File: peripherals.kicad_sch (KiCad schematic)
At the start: 39 parts, among them J12 PinHeader_2x5_P1.27mm_SMD, J13 PinHeader_2x5_P1.27mm_SMD, J14 PinHeader_2x5_P1.27mm_SMD, J15 PinHeader_2x5_P1.27mm_SMD, J16 PinHeader_2x5_P1.27mm_SMD, J20 PinHeader_2x5_P1.27mm_SMD, J6 PinHeader_2x10_P1.27mm_SMD_Sh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, J7 JST_SH_1x4_BM04B-SRSS-TB-LF-SN, J8 PinHeader_1x2_P1.27mm_Drill0.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, J9 PinHeader_2x5_P1.27mm_SMD_Shr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, Q2 DMG1012T-7, Q3 DMG1012T-7, Q4 DMG1012T-7, U1 TMP75AIDR, U2 AT24C04C_SOIC8

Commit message: [#93514] Add separating lines, clean schematics
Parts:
- added R57: R_100k_0402, antmicro-footprints:R_0402_1005Metric, symbol antmicroResistors0402:R_100k_0402
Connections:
- net GND: now also R57.1; no longer Q4.1 (G)
- new net ~{DC_SCM_SPI_SCMCNTRL_IRQ0}: Q4.1 (G), R57.2
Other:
- moved on the sheet: C5, C6, D11, D7, J8, J9, Q4, R11, R13, R2, R21, R22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

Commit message: [#93514] Align items to grid, add NC-SI testpads
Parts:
- added TP17, TP18, TP19, TP20, TP21, TP22, TP23: TP_0.75mm_SMD, antmicro-footprints:TP_SMD_0.75mm, symbol antmicroTestPoints:TP_0.75mm_SMD
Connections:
- new net DC_SCM_NC-SI.CRS_DV: TP18.1
- new net DC_SCM_NC-SI.REF_CLK: TP17.1
- new net DC_SCM_NC-SI.RXD0: TP19.1
- new net DC_SCM_NC-SI.RXD1: TP20.1
- new net DC_SCM_NC-SI.TXD0: TP22.1
- new net DC_SCM_NC-SI.TXD1: TP23.1
- new net DC_SCM_NC-SI.TX_EN: TP21.1
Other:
- note added: "NC-SI"
- moved on the sheet: D3, J20, J7, R18, R19

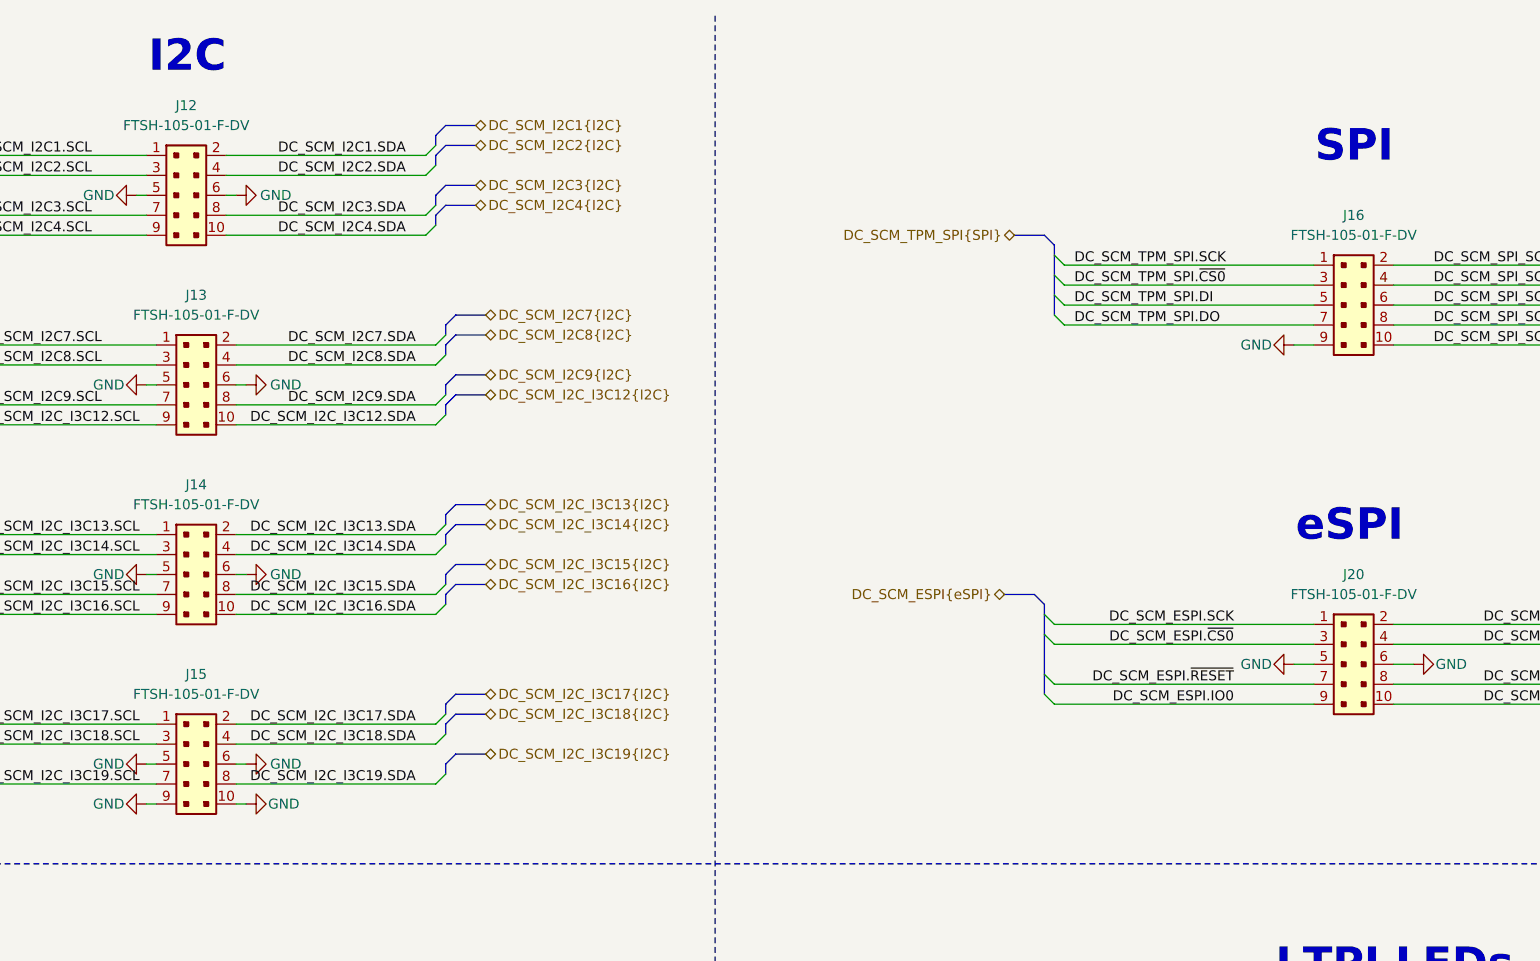
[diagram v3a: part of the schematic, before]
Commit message: [#93514] Add dnp to SPI, eSPI components testpads
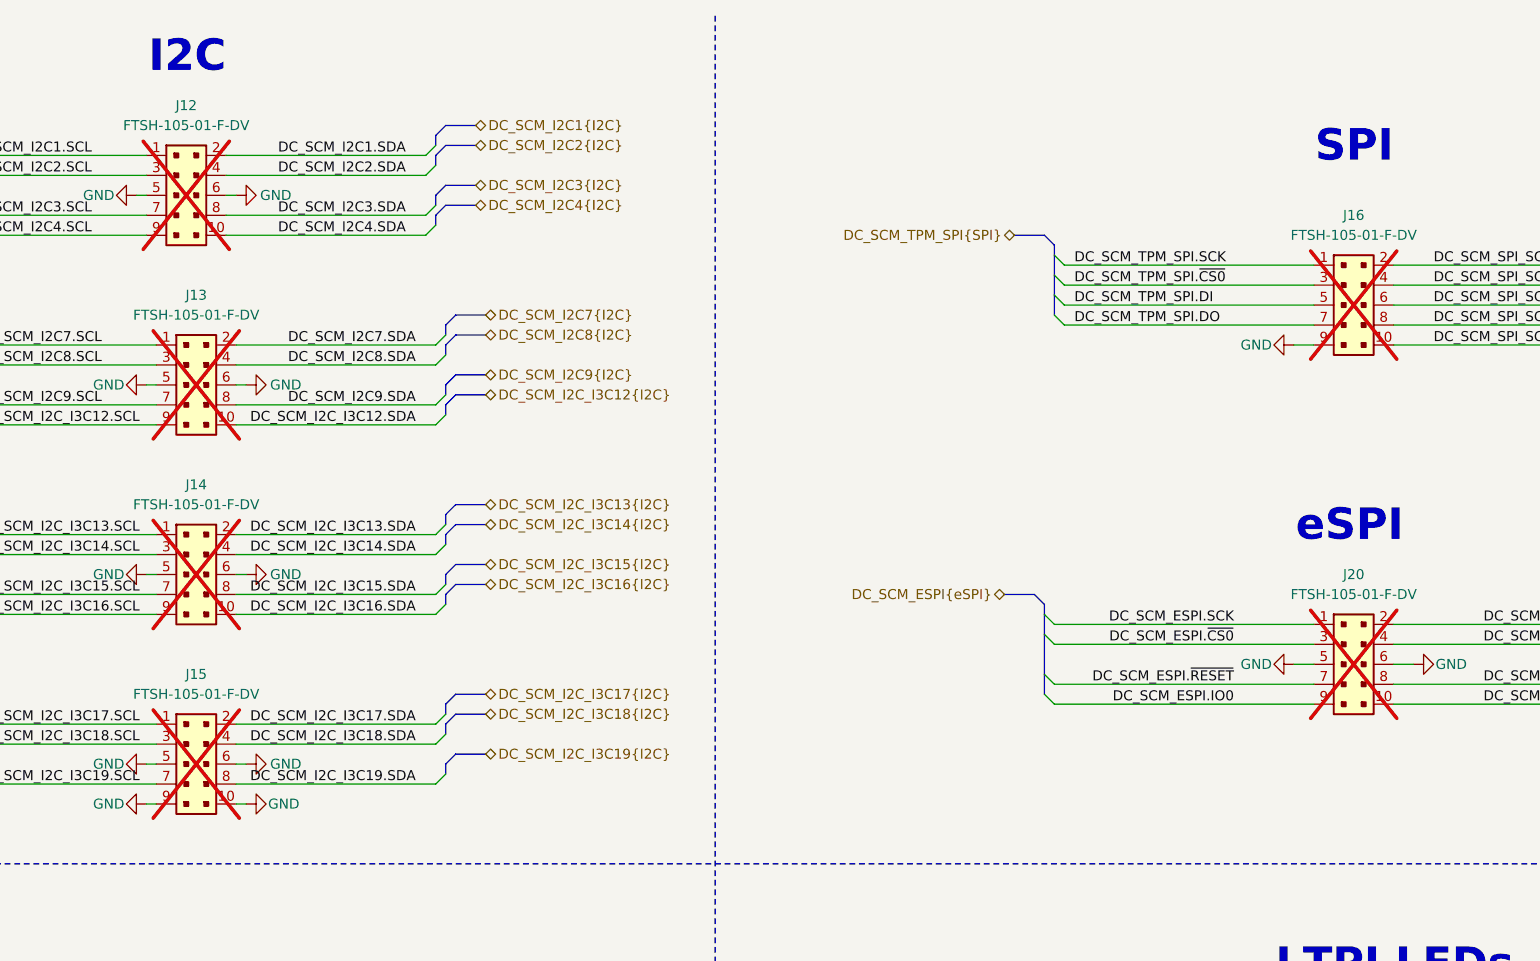
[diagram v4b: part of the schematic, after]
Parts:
- J12, J13, J14, J15, J16, J20: now not fitted
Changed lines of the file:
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@@
 		(in_bom yes)
 		(on_board yes)
-		(dnp no)
+		(dnp yes)
 		(fields_autoplaced yes)
 		(property "Reference" "J13"
@@
 		(in_bom yes)
 		(on_board yes)
-		(dnp no)
+		(dnp yes)
 		(fields_autoplaced yes)
 		(property "Reference" "J15"
@@
 		(in_bom yes)
 		(on_board yes)
-		(dnp no)
+		(dnp yes)
 		(fields_autoplaced yes)
 		(property "Reference" "J20"
@@
 		(in_bom yes)
 		(on_board yes)
-		(dnp no)
+		(dnp yes)
 		(fields_autoplaced yes)
 		(property "Reference" "J14"
@@
 		(in_bom yes)
 		(on_board yes)
-		(dnp no)
+		(dnp yes)
 		(fields_autoplaced yes)
 		(property "Reference" "J16"
@@
 		(in_bom yes)
 		(on_board yes)
-		(dnp no)
+		(dnp yes)
 		(fields_autoplaced yes)
 		(property "Reference" "J12"

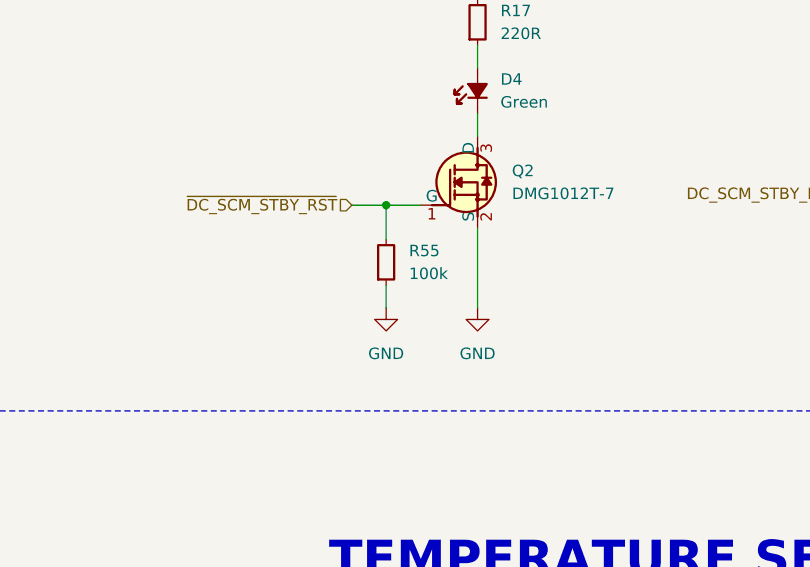
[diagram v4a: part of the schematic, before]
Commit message: [#93514] Leave one pull-down for DC_SCM_STBY_RST
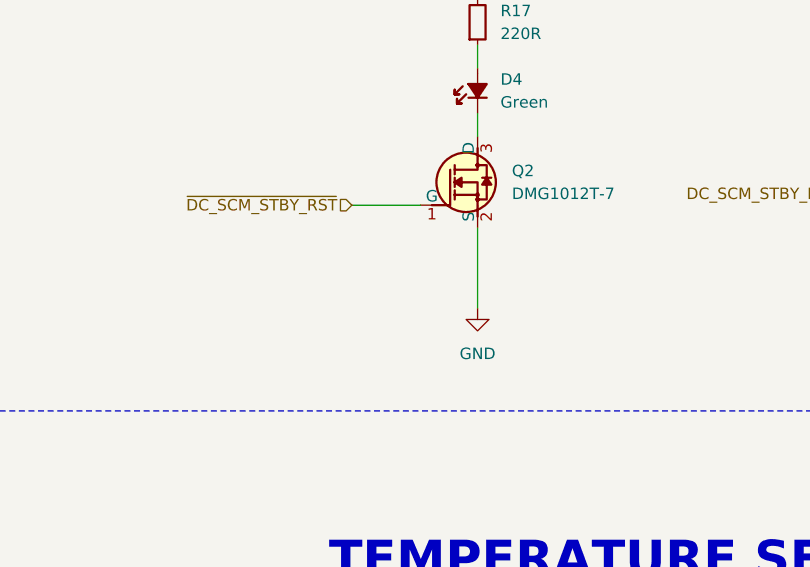
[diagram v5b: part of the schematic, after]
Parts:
- removed R55: R_100k_0402, antmicro-footprints:R_0402_1005Metric, symbol antmicroResistors0402:R_100k_0402

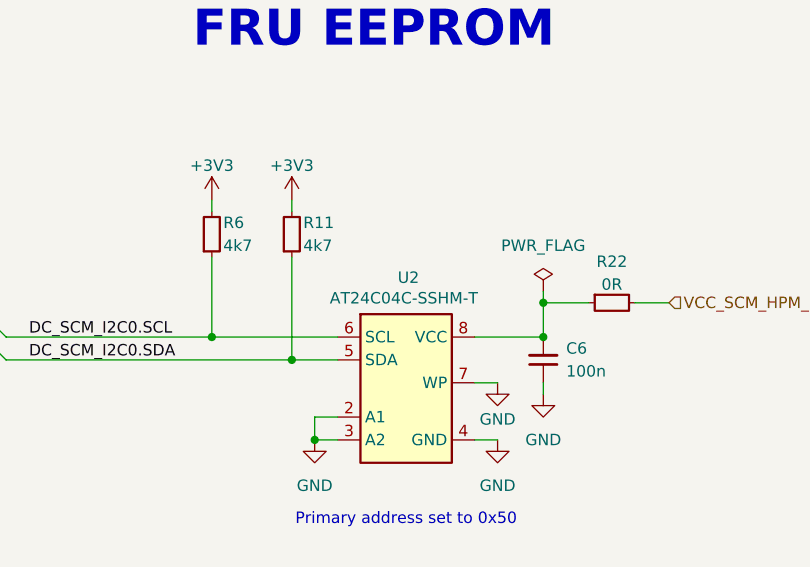
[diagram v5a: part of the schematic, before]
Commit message: [#93514] Replace old AT24C04C
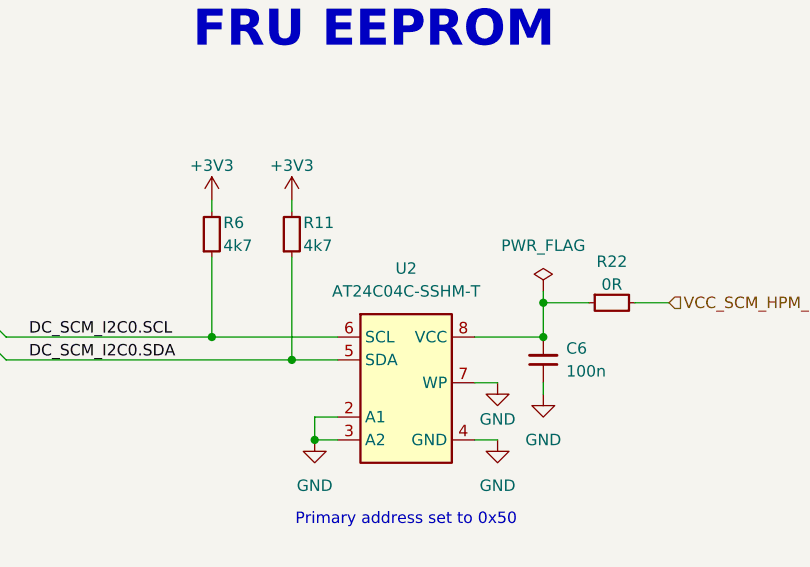
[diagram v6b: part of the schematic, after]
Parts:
- U2: MPN AT24C04C-SSHM-T -> AT24C04C-SSHM-T
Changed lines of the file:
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@@
-	)
-	(symbol
-		(lib_id "antmicroMemory:AT24C04C_SOIC8")
-		(at 77.47 245.11 0)
-		(unit 1)
-		(exclude_from_sim no)
-		(in_bom yes)
-		(on_board yes)
-		(dnp no)
-		(property "Reference" "U2"
-			(at 85.344 238.506 0)
-			(effects
-				(font
-					(size 1.27 1.27)
-					(thickness 0.15)
-				)
-			)
-		)
-		(property "Value" "AT24C04C_SOIC8"
-			(at 113.03 250.19 0)
-			(effects
-				(font
-					(size 1.27 1.27)
-					(thickness 0.15)
-				)
-				(justify left bottom)
-				(hide yes)
-			)
-		)
-		(property "Footprint" "antmicro-footprints:SOIC-8_3.9x4.9x1.75mm_P1.27mm"
-			(at 113.03 252.73 0)
-			(effects
-				(font
-					(size 1.27 1.27)
-					(thickness 0.15)
-				)
-				(justify left bottom)
-				(hide yes)
-			)
-		)
-		(property "Datasheet" "https://www.mouser.co.uk/datasheet/3/282/1/AT24C04C-AT24C08C-I2C-Compatible-Two-Wire-Serial-EEPROM-4-Kbit-8-Kbit-20006127.pdf"
-			(at 113.03 255.27 0)
-			(effects
-				(font
-					(size 1.27 1.27)
-					(thickness 0.15)
-				)
-				(justify left bottom)
-				(hide yes)
-			)
-		)
-		(property "Description" "EEPROM, 4 Kbit, 512 x 8bit, Serial I2C (2-Wire), 1 MHz, SOIC-8"
-			(at 113.03 267.97 0)
-			(effects
-				(font
-					(size 1.27 1.27)
-				)
-				(justify left bottom)
-				(hide yes)
-			)
-		)
-		(property "Manufacturer" "Microchip Technology"
-			(at 113.03 257.81 0)
-			(effects
-				(font
-					(size 1.27 1.27)
-					(thickness 0.15)
-				)
-				(justify left bottom)
-				(hide yes)
-			)
-		)
-		(property "MPN" " AT24C04C-SSHM-T "
-			(at 84.836 240.792 0)
-			(effects
-				(font
-					(size 1.27 1.27)
-					(thickness 0.15)
-				)
-			)
-		)
-		(property "Author" "Antmicro"
-			(at 113.03 262.89 0)
-			(effects
-				(font
-					(size 1.27 1.27)
-					(thickness 0.15)
-				)
-				(justify left bottom)
-				(hide yes)
-			)
-		)
-		(property "License" "Apache-2.0"
-			(at 113.03 265.43 0)
-			(effects
-				(font
-					(size 1.27 1.27)
-					(thickness 0.15)
-				)
-				(justify left bottom)
-				(hide yes)
-			)
-		)
-		(pin "6"
-		)
-		(pin "5"
-		)
-		(pin "7"
-		)
-		(pin "8"
-		)
-		(pin "1"
-		)
-		(pin "3"
-		)
-		(pin "2"
-		)
-		(pin "4"
-		)
-		(instances
-			(project "bmc-breakout-board"
-				(path "/5d67ef28-5805-4f87-b722-2926dabf7f6e/f1ecdd24-c7ef-4765-8186-53d06f23944d"
-					(reference "U2")
-					(unit 1)
-				)
-			)
-		)
 	)
 	(symbol
@@
 					(unit 1)
 				)
+			)
+		)
+	)
+	(symbol
+		(lib_id "antmicroMemory:AT24C04C_SOIC8")
+		(at 77.47 245.11 0)
+		(unit 1)
+		(exclude_from_sim no)
+		(in_bom yes)
+		(on_board yes)
+		(dnp no)
+		(fields_autoplaced yes)
+		(property "Reference" "U2"
+			(at 85.09 237.49 0)
+			(effects
+				(font
+					(size 1.27 1.27)
+					(thickness 0.15)
+				)
+			)
+		)
+		(property "Value" "AT24C04C_SOIC8"
+			(at 113.03 250.19 0)
+			(effects
+				(font
+					(size 1.27 1.27)
+					(thickness 0.15)
+				)
+				(justify left bottom)
+				(hide yes)
+			)
+		)
+		(property "Footprint" "antmicro-footprints:SOIC-8_3.9x4.9x1.75mm_P1.27mm"
+			(at 113.03 252.73 0)
+			(effects
+				(font
+					(size 1.27 1.27)
+					(thickness 0.15)
+				)
+				(justify left bottom)
+				(hide yes)
+			)
+		)
+		(property "Datasheet" "https://www.mouser.co.uk/datasheet/3/282/1/AT24C04C-AT24C08C-I2C-Compatible-Two-Wire-Serial-EEPROM-4-Kbit-8-Kbit-20006127.pdf"
+			(at 113.03 255.27 0)
+			(effects
+				(font
+					(size 1.27 1.27)
+					(thickness 0.15)
+				)
+				(justify left bottom)
+				(hide yes)
+			)
+		)
+		(property "Description" "EEPROM, 4 Kbit, 512 x 8bit, Serial I2C (2-Wire), 1 MHz, SOIC-8"
+			(at 113.03 267.97 0)
+			(effects
+				(font
+					(size 1.27 1.27)
+				)
+				(justify left bottom)
+				(hide yes)
+			)
+		)
+		(property "Manufacturer" "Microchip Technology"
+			(at 113.03 257.81 0)
+			(effects
+				(font
+					(size 1.27 1.27)
+					(thickness 0.15)
+				)
+				(justify left bottom)
+				(hide yes)
+			)
+		)
+		(property "MPN" "AT24C04C-SSHM-T"
+			(at 85.09 240.03 0)
+			(effects
+				(font
+					(size 1.27 1.27)
+					(thickness 0.15)
+				)
+			)
+		)
+		(property "Author" "Antmicro"
+			(at 113.03 262.89 0)
+			(effects
+				(font
+					(size 1.27 1.27)
+					(thickness 0.15)
+				)
+				(justify left bottom)
+				(hide yes)
+			)
+		)
+		(property "License" "Apache-2.0"
+			(at 113.03 265.43 0)
+			(effects
+				(font
+					(size 1.27 1.27)
+					(thickness 0.15)
+				)
+				(justify left bottom)
+				(hide yes)
+			)
+		)
+		(pin "1"
+		)
+		(pin "3"
+		)
+		(pin "8"
+		)
+		(pin "7"
+		)
+		(pin "4"
+		)
+		(pin "2"
+		)
+		(pin "6"
+		)
+		(pin "5"
+		)
+		(instances
+			(project "bmc-breakout-board"
+				(path "/5d67ef28-5805-4f87-b722-2926dabf7f6e/f1ecdd24-c7ef-4765-8186-53d06f23944d"
+					(reference "U2")
+					(unit 1)
+				)

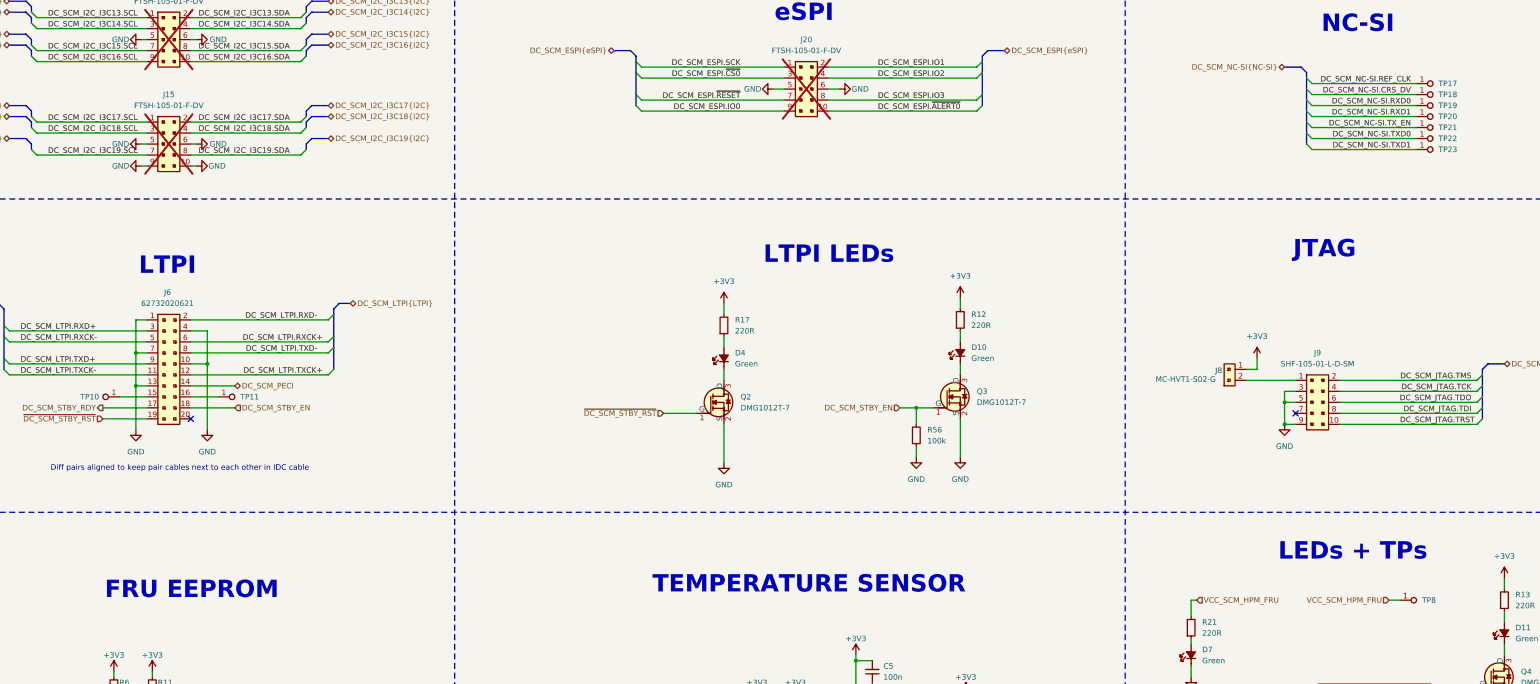
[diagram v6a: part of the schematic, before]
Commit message: [#93949] Change testpads to 1.5mm, change QSPI and UART testpad to smd technology
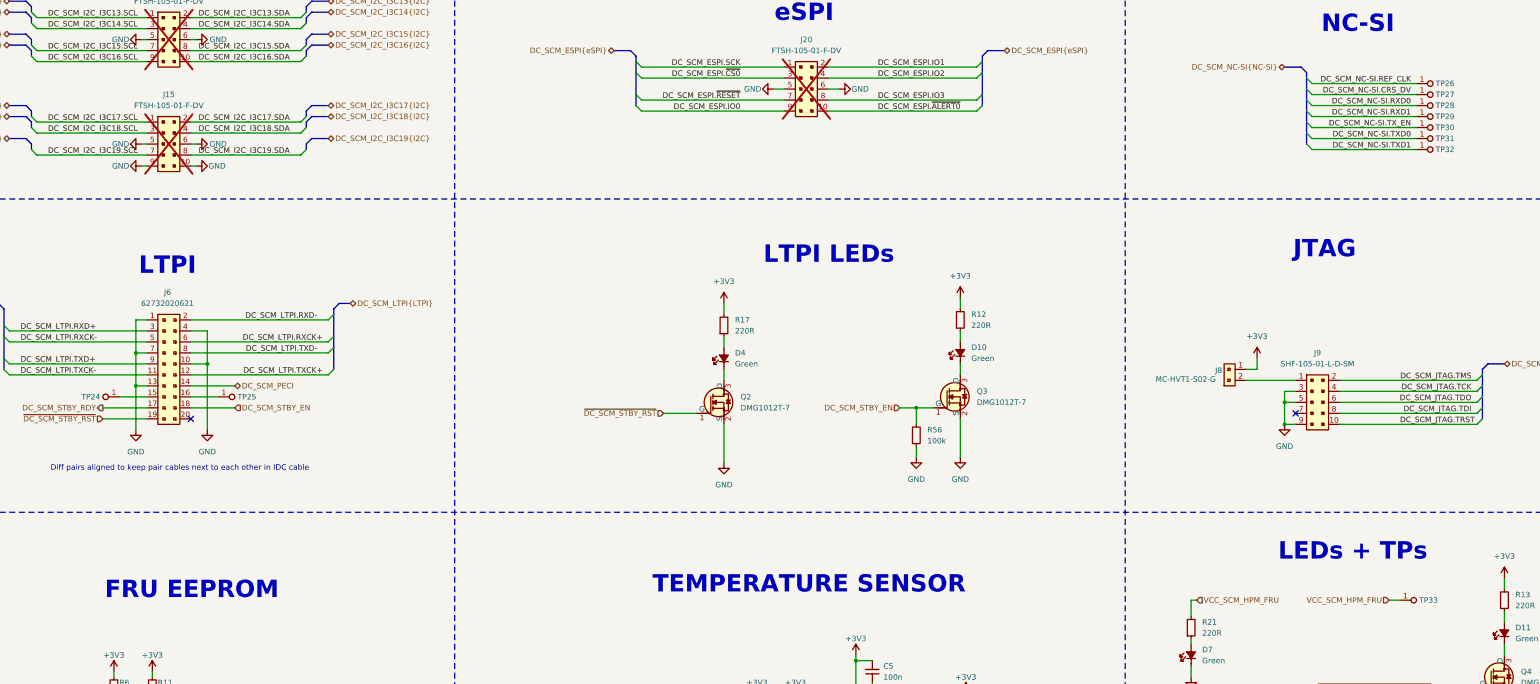
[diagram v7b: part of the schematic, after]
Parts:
- removed TP10, TP11, TP17, TP18, TP19, TP20, TP21, TP22, TP23, TP8: TP_0.75mm_SMD, antmicro-footprints:TP_SMD_0.75mm, symbol antmicroTestPoints:TP_0.75mm_SMD
- added TP24, TP25, TP26, TP27, TP28, TP29, TP30, TP31, TP32, TP33: TP_1.5mm_SMD, antmicro-footprints:TP_SMD_1.5mm, symbol antmicroTestPoints:TP_1.5mm_SMD
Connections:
- net DC_SCM_NC-SI.CRS_DV: now also TP27.1
- net DC_SCM_NC-SI.REF_CLK: now also TP26.1
- net DC_SCM_NC-SI.RXD0: now also TP28.1
- net DC_SCM_NC-SI.RXD1: now also TP29.1
- net DC_SCM_NC-SI.TXD0: now also TP31.1
- net DC_SCM_NC-SI.TXD1: now also TP32.1
- net DC_SCM_NC-SI.TX_EN: now also TP30.1
- net VCC_SCM_HPM_FRU: now also TP33.1
- net at J6.15: now also TP24.1
- net at J6.16: now also TP25.1
